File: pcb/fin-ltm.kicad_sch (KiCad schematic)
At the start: 68 parts, among them J1 Connector, USB-TYPE-C-16P, J2 Test Connector, J3 Display, Q1 MMBT3904, Q2 HL3415A, U1 ESP32-C3FH4, U2 RT9080, U3 SN74LV1T34DBV, X1 40MHz, 15pF

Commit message: pcb 2
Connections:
- net BRIGHTNESS_DOWN_BUTTON: now also R16.2, U1.15 (GPIO9); no longer R17.2, U1.16 (GPIO10)
- net BRIGHTNESS_UP_BUTTON: now also R17.2, U1.16 (GPIO10); no longer R16.2, U1.15 (GPIO9)
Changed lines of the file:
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@@
+	(wire
+		(pts
+			(xy 165.1 116.84) (xy 166.37 116.84)
+		)
+		(stroke
+			(width 0)
+			(type default)
+		)
+	)
+	(wire
+		(pts
+			(xy 236.22 34.29) (xy 236.22 35.56)
+		)
+		(stroke
+			(width 0)
+			(type default)
+		)
+	)
+	(wire
+		(pts
+			(xy 181.61 43.18) (xy 208.28 43.18)
+		)
+		(stroke
+			(width 0)
+			(type default)
+		)
+	)
 	(wire
 		(pts
 			(xy 165.1 50.8) (xy 208.28 50.8)
-		)
-		(stroke
-			(width 0)
-			(type default)
-		)
-	)
-	(wire
-		(pts
-			(xy 165.1 116.84) (xy 166.37 116.84)
-		)
-		(stroke
-			(width 0)
-			(type default)
-		)
-	)
-	(wire
-		(pts
-			(xy 236.22 34.29) (xy 236.22 35.56)
-		)
-		(stroke
-			(width 0)
-			(type default)
-		)
-	)
-	(wire
-		(pts
-			(xy 181.61 43.18) (xy 208.28 43.18)
 		)
 		(stroke
@@
 	)
 	(label "BRIGHTNESS_DOWN_BUTTON"
-		(at 181.61 50.8 0)
+		(at 181.61 48.26 0)
 		(effects
 			(font
@@
 	)
 	(label "BRIGHTNESS_UP_BUTTON"
-		(at 181.61 48.26 0)
-		(effects
-			(font
+		(at 181.61 50.8 0)
+		(effects
+			(font

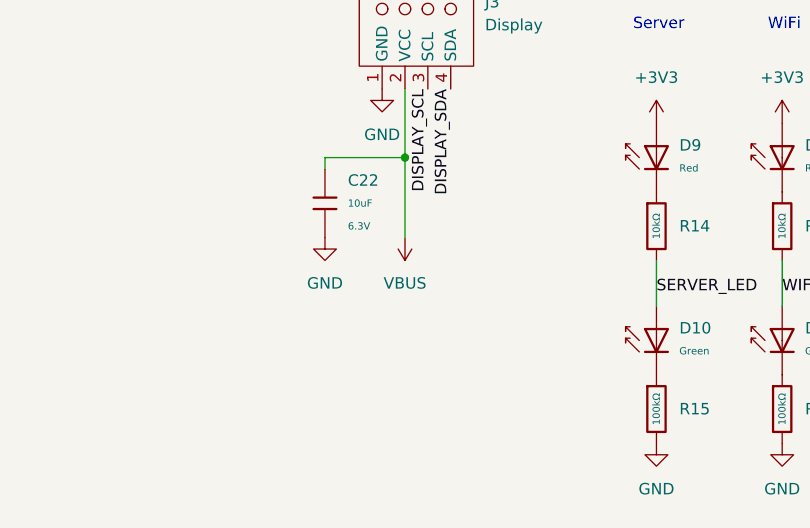
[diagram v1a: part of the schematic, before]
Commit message: add oled
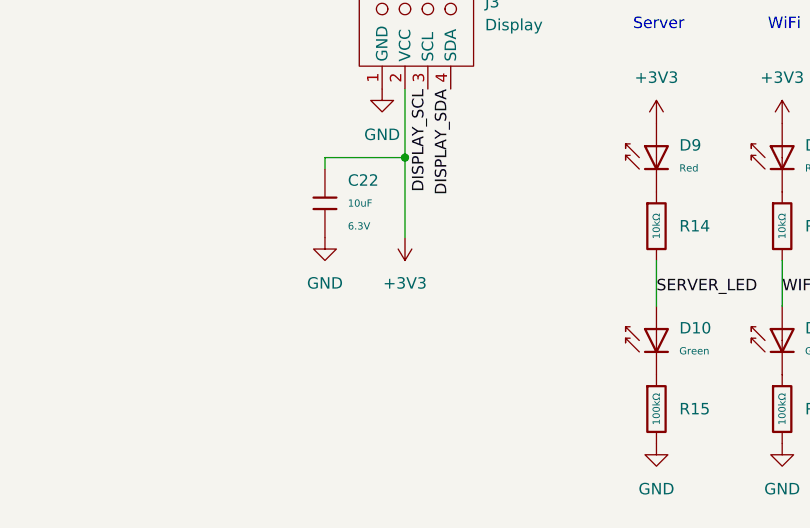
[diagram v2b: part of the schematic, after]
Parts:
- AE1: footprint Library:Inverted_F_Antenna_2.4Ghz_1.0mmPCB_TI_CC2430DB.pretty -> Custom:Inverted_F_Antenna_2.4Ghz_1.0mmPCB_TI_CC2430DB.pretty
- J2: footprint Library:Test_connector -> Custom:Test_connector
- J3: footprint (none) -> Custom:OLED_1306_THT_pinheader
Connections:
- net +3V3: now also C22.1, J3.2 (VCC)
- net VBUS: no longer C22.1, J3.2 (VCC)
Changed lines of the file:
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@@
 			)
 		)
-		(property "Footprint" "Library:Test_connector"
+		(property "Footprint" "Custom:Test_connector"
 			(at 269.24 106.68 0)
 			(hide yes)
@@
 	)
 	(symbol
+		(lib_id "power:+3V3")
+		(at 87.63 160.02 180)
+		(unit 1)
+		(body_style 1)
+		(exclude_from_sim no)
+		(in_bom yes)
+		(on_board yes)
+		(in_pos_files yes)
+		(dnp no)
+		(fields_autoplaced yes)
+		(property "Reference" "#PWR0302"
+			(at 87.63 156.21 0)
+			(hide yes)
+			(show_name no)
+			(do_not_autoplace no)
+			(effects
+				(font
+					(size 1.27 1.27)
+				)
+			)
+		)
+		(property "Value" "+3V3"
+			(at 87.63 165.1 0)
+			(show_name no)
+			(do_not_autoplace no)
+			(effects
+				(font
+					(size 1.27 1.27)
+				)
+			)
+		)
+		(property "Footprint" ""
+			(at 87.63 160.02 0)
+			(hide yes)
+			(show_name no)
+			(do_not_autoplace no)
+			(effects
+				(font
+					(size 1.27 1.27)
+				)
+			)
+		)
+		(property "Datasheet" ""
+			(at 87.63 160.02 0)
+			(hide yes)
+			(show_name no)
+			(do_not_autoplace no)
+			(effects
+				(font
+					(size 1.27 1.27)
+				)
+			)
+		)
+		(property "Description" "Power symbol creates a global label with name \"+3V3\""
+			(at 87.63 160.02 0)
+			(hide yes)
+			(show_name no)
+			(do_not_autoplace no)
+			(effects
+				(font
+					(size 1.27 1.27)
+				)
+			)
+		)
+		(pin "1"
+		)
+		(instances
+			(project "fin-ltm"
+				(path "/da13f94e-0fc0-403b-a3ae-59c6a026d422"
+					(reference "#PWR0302")
+					(unit 1)
+				)
+			)
+		)
+	)
+	(symbol
 		(lib_id "power:GND")
 		(at 165.1 124.46 0)
@@
 			)
 		)
-		(property "Footprint" "Library:Inverted_F_Antenna_2.4Ghz_1.0mmPCB_TI_CC2430DB.pretty"
+		(property "Footprint" "Custom:Inverted_F_Antenna_2.4Ghz_1.0mmPCB_TI_CC2430DB.pretty"
 			(at 194.31 109.22 0)
 			(hide yes)
@@
 			)
 		)
-		(property "Footprint" ""
+		(property "Footprint" "Custom:OLED_1306_THT_pinheader"
 			(at 88.9 140.97 0)
 			(hide yes)
@@
 					(unit 1)
 				)
-			)
-		)
-	)
-	(symbol
-		(lib_id "power:VBUS")
-		(at 87.63 160.02 180)
-		(unit 1)
-		(body_style 1)
-		(exclude_from_sim no)
-		(in_bom yes)
-		(on_board yes)
-		(in_pos_files yes)
-		(dnp no)
-		(fields_autoplaced yes)
-		(property "Reference" "#PWR075"
-			(at 87.63 156.21 0)
-			(hide yes)
-			(show_name no)
-			(do_not_autoplace no)
-			(effects
-				(font
-					(size 1.27 1.27)
-				)
-			)
-		)
-		(property "Value" "VBUS"
-			(at 87.63 165.1 0)
-			(show_name no)
-			(do_not_autoplace no)
-			(effects
-				(font
-					(size 1.27 1.27)
-				)
-			)
-		)
-		(property "Footprint" ""
-			(at 87.63 160.02 0)
-			(hide yes)
-			(show_name no)
-			(do_not_autoplace no)
-			(effects
-				(font
-					(size 1.27 1.27)
-				)
-			)
-		)
-		(property "Datasheet" ""
-			(at 87.63 160.02 0)
-			(hide yes)
-			(show_name no)
-			(do_not_autoplace no)
-			(effects
-				(font
-					(size 1.27 1.27)
-				)
-			)
-		)
-		(property "Description" "Power symbol creates a global label with name \"VBUS\""
-			(at 87.63 160.02 0)
-			(hide yes)
-			(show_name no)
-			(do_not_autoplace no)
-			(effects
-				(font
-					(size 1.27 1.27)
-				)
-			)
-		)
-		(pin "1"
-		)
-		(instances
-			(project "fin-ltm"
-				(path "/da13f94e-0fc0-403b-a3ae-59c6a026d422"
-					(reference "#PWR075")
-					(unit 1)
-				)

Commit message: led routing
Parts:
- removed C22: 10uF, PCM_JLCPCB:C_0402, symbol PCM_JLCPCB-Capacitors:0402,10uF
- removed J3: Display, Custom:OLED_1306_THT_pinheader, symbol New_Library:SSD1306_Conn
- removed R18, R19: 10kΩ, PCM_JLCPCB:R_0402, symbol PCM_JLCPCB-Resistors:0402,10kΩ
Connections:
- net DISPLAY_SCL: no longer names the net of U1.5 (GPIO1/XTAL_32K_N)
- net DISPLAY_SDA: no longer names the net of U1.4 (GPIO0/XTAL_32K_P)

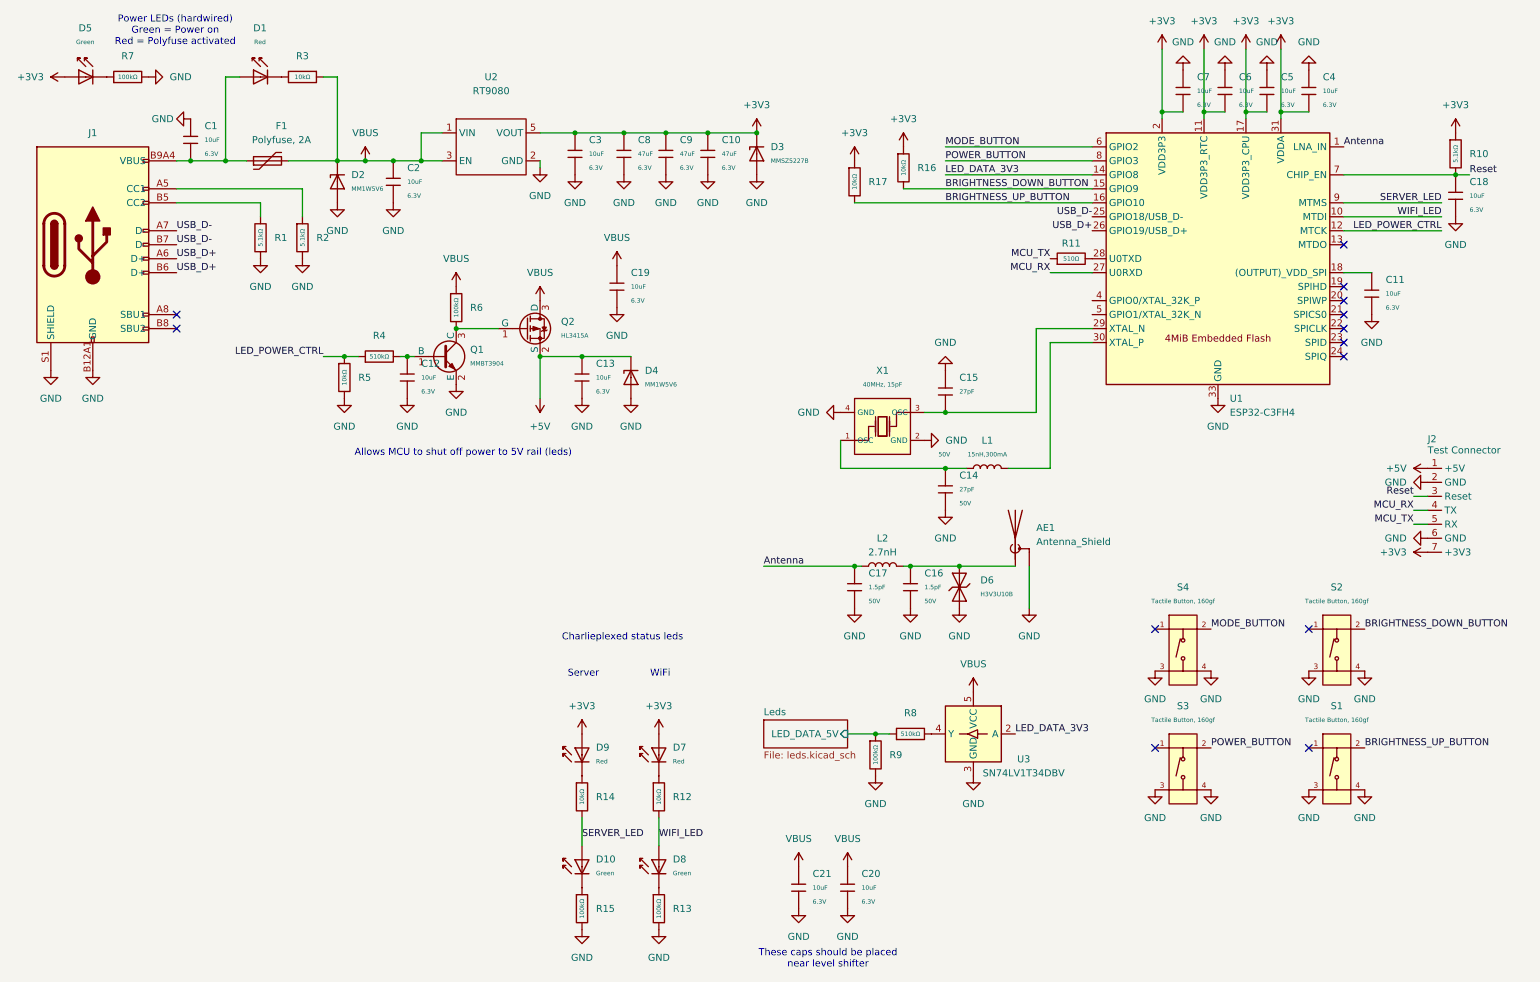
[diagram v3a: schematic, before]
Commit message: linking leds to stations
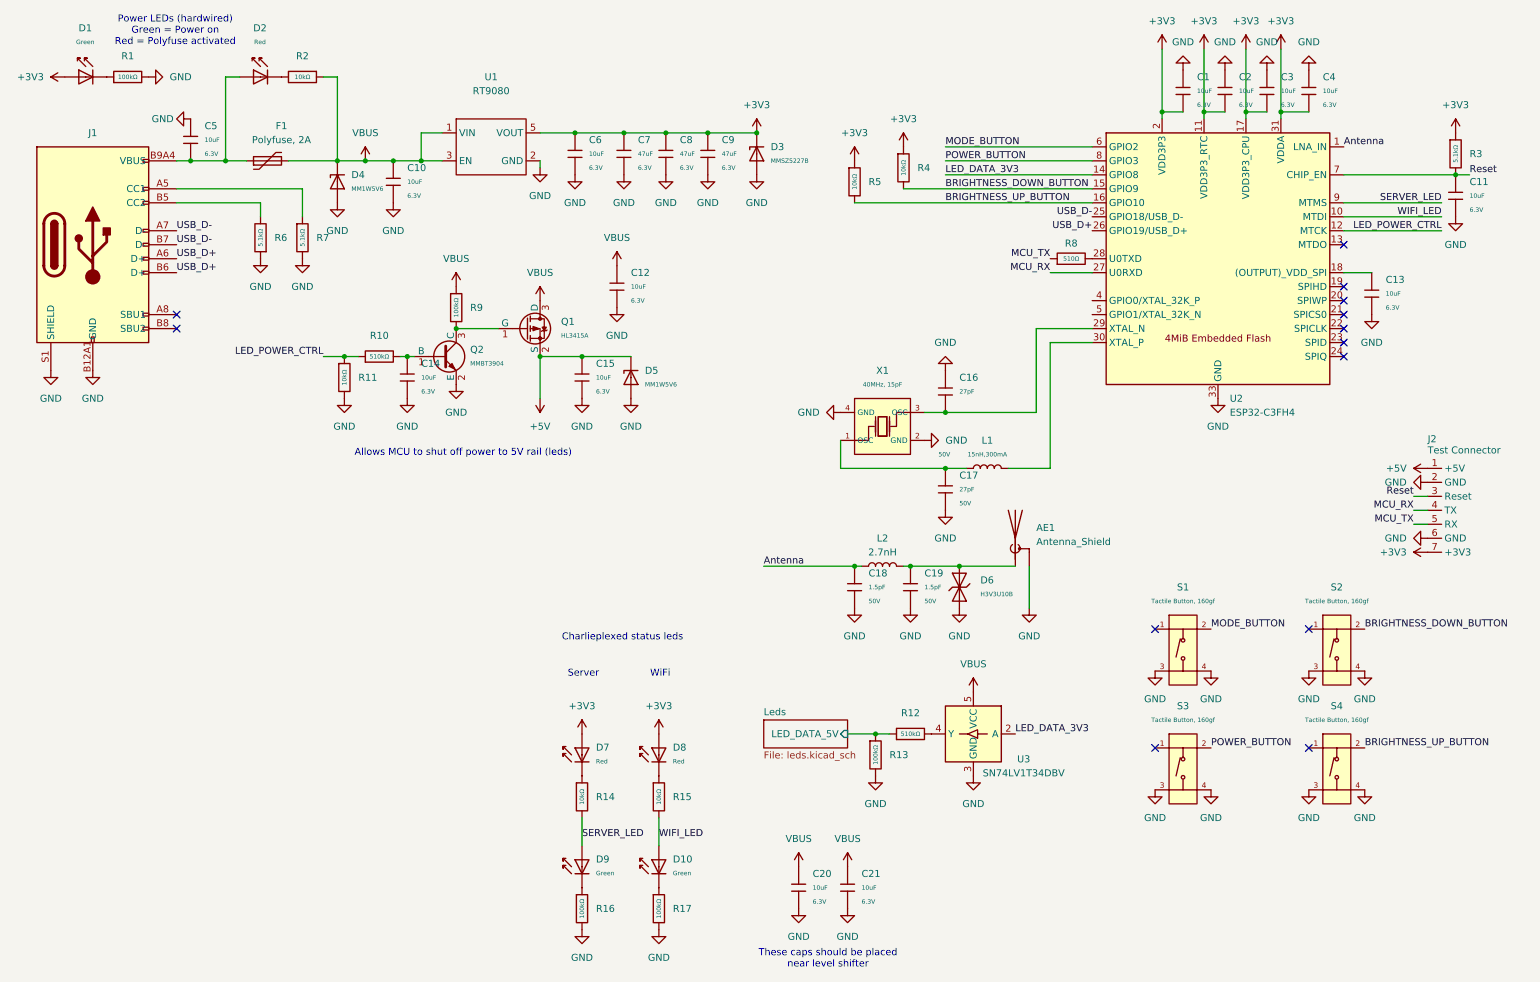
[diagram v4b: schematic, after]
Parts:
- renumbered C7 to C1, C2 to C10, C18 to C11, C19 to C12, C11 to C13, C12 to C14, C13 to C15, C15 to C16, C14 to C17, C17 to C18, C16 to C19, C6 to C2, C21 to C20, C20 to C21, C5 to C3, C1 to C5, C3 to C6, C8 to C7, C9 to C8, C10 to C9, D5 to D1, D8 to D10, D1 to D2, D2 to D4, D4 to D5, D9 to D7, D7 to D8, D10 to D9, Q2 to Q1, Q1 to Q2, R7 to R1, R4 to R10, R5 to R11, R8 to R12, R9 to R13, R12 to R15, R15 to R16, R13 to R17, R3 to R2, R10 to R3, R16 to R4, R17 to R5, R1 to R6, R2 to R7, R11 to R8, R6 to R9, S4 to S1, S1 to S4, U2 to U1, U1 to U2

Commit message: pcb finished
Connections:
- no-connect marks 13 -> 15
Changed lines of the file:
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@@
+	)
+	(no_connect
+		(at 208.28 68.58)
 	)
 	(no_connect
@@
 	)
 	(no_connect
+		(at 208.28 71.12)
+	)
+	(no_connect

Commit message: finished pcb
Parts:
- C10, C12, C20, C21, C5: footprint PCM_JLCPCB:C_0402 -> PCM_JLCPCB:C_0603; symbol PCM_JLCPCB-Capacitors:0402,10uF -> PCM_JLCPCB-Capacitors:0603,10uF; LCSC C15525 -> C19702; Part CL05A106MQ5NUNC -> CL10A106KP8NNNC; Stock 3940889 -> 9881407; Tolerance ±20% -> ±10%; Voltage Rated 6.3V -> 10V
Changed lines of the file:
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@@
 	)
 	(symbol
-		(lib_id "PCM_JLCPCB-Capacitors:0402,10uF")
+		(lib_id "PCM_JLCPCB-Capacitors:0603,10uF")
 		(at 154.94 175.26 0)
 		(unit 1)
@@
 			)
 		)
-		(property "Footprint" "PCM_JLCPCB:C_0402"
+		(property "Footprint" "PCM_JLCPCB:C_0603"
 			(at 153.162 175.26 90)
 			(hide yes)
@@
 			)
 		)
-		(property "Datasheet" "https://www.lcsc.com/datasheet/lcsc_datasheet_2208231630_Samsung-Electro-Mechanics-CL05A106MQ5NUNC_C15525.pdf"
+		(property "Datasheet" "https://www.lcsc.com/datasheet/lcsc_datasheet_2304140030_Samsung-Electro-Mechanics-CL10A106KP8NNNC_C19702.pdf"
 			(at 154.94 175.26 0)
 			(hide yes)
@@
 			)
 		)
-		(property "Description" "6.3V 10uF X5R ±20% 0402 Multilayer Ceramic Capacitors MLCC - SMD/SMT ROHS"
+		(property "Description" "10V 10uF X5R ±10% 0603 Multilayer Ceramic Capacitors MLCC - SMD/SMT ROHS"
 			(at 154.94 175.26 0)
 			(hide yes)
@@
 			)
 		)
-		(property "LCSC" "C15525"
+		(property "LCSC" "C19702"
 			(at 154.94 175.26 0)
 			(hide yes)
@@
 			)
 		)
-		(property "Stock" "3940889"
+		(property "Stock" "9881407"
 			(at 154.94 175.26 0)
 			(hide yes)
@@
 			)
 		)
-		(property "Part" "CL05A106MQ5NUNC"
+		(property "Part" "CL10A106KP8NNNC"
 			(at 154.94 175.26 0)
 			(hide yes)
@@
 			)
 		)
-		(property "Voltage Rated" "6.3V"
+		(property "Voltage Rated" "10V"
 			(at 157.48 177.8 0)
 			(show_name no)
@@
 			)
 		)
-		(property "Tolerance" "±20%"
+		(property "Tolerance" "±10%"
 			(at 154.94 175.26 0)
 			(hide yes)
@@
 	)
 	(symbol
-		(lib_id "PCM_JLCPCB-Capacitors:0402,10uF")
+		(lib_id "PCM_JLCPCB-Capacitors:0603,10uF")
 		(at 163.83 175.26 0)
 		(unit 1)
@@
 			)
 		)
-		(property "Footprint" "PCM_JLCPCB:C_0402"
+		(property "Footprint" "PCM_JLCPCB:C_0603"
 			(at 162.052 175.26 90)
 			(hide yes)
@@
 			)
 		)
-		(property "Datasheet" "https://www.lcsc.com/datasheet/lcsc_datasheet_2208231630_Samsung-Electro-Mechanics-CL05A106MQ5NUNC_C15525.pdf"
+		(property "Datasheet" "https://www.lcsc.com/datasheet/lcsc_datasheet_2304140030_Samsung-Electro-Mechanics-CL10A106KP8NNNC_C19702.pdf"
 			(at 163.83 175.26 0)
 			(hide yes)
@@
 			)
 		)
-		(property "Description" "6.3V 10uF X5R ±20% 0402 Multilayer Ceramic Capacitors MLCC - SMD/SMT ROHS"
+		(property "Description" "10V 10uF X5R ±10% 0603 Multilayer Ceramic Capacitors MLCC - SMD/SMT ROHS"
 			(at 163.83 175.26 0)
 			(hide yes)
@@
 			)
 		)
-		(property "LCSC" "C15525"
+		(property "LCSC" "C19702"
 			(at 163.83 175.26 0)
 			(hide yes)
@@
 			)
 		)
-		(property "Stock" "3940889"
+		(property "Stock" "9881407"
 			(at 163.83 175.26 0)
 			(hide yes)
@@
 			)
 		)
-		(property "Part" "CL05A106MQ5NUNC"
+		(property "Part" "CL10A106KP8NNNC"
 			(at 163.83 175.26 0)
 			(hide yes)
@@
 			)
 		)
-		(property "Voltage Rated" "6.3V"
+		(property "Voltage Rated" "10V"
 			(at 166.37 177.8 0)
 			(show_name no)
@@
 			)
 		)
-		(property "Tolerance" "±20%"
+		(property "Tolerance" "±10%"
 			(at 163.83 175.26 0)
 			(hide yes)
@@
 	)
 	(symbol
-		(lib_id "PCM_JLCPCB-Capacitors:0402,10uF")
+		(lib_id "PCM_JLCPCB-Capacitors:0603,10uF")
 		(at 81.28 46.99 0)
 		(unit 1)
@@
 		)
 		(property "Value" "10uF"
-			(at 83.82 46.99 0)
+			(at 83.312 47.3682 0)
 			(show_name no)
 			(do_not_autoplace no)
@@
 			)
 		)
-		(property "Footprint" "PCM_JLCPCB:C_0402"
+		(property "Footprint" "PCM_JLCPCB:C_0603"
 			(at 79.502 46.99 90)
 			(hide yes)
@@
 			)
 		)
-		(property "Datasheet" "https://www.lcsc.com/datasheet/lcsc_datasheet_2208231630_Samsung-Electro-Mechanics-CL05A106MQ5NUNC_C15525.pdf"
+		(property "Datasheet" "https://www.lcsc.com/datasheet/lcsc_datasheet_2304140030_Samsung-Electro-Mechanics-CL10A106KP8NNNC_C19702.pdf"
 			(at 81.28 46.99 0)
 			(hide yes)
@@
 			)
 		)
-		(property "Description" "6.3V 10uF X5R ±20% 0402 Multilayer Ceramic Capacitors MLCC - SMD/SMT ROHS"
+		(property "Description" "10V 10uF X5R ±10% 0603 Multilayer Ceramic Capacitors MLCC - SMD/SMT ROHS"
 			(at 81.28 46.99 0)
 			(hide yes)
@@
 			)
 		)
-		(property "LCSC" "C15525"
+		(property "LCSC" "C19702"
 			(at 81.28 46.99 0)
 			(hide yes)
@@
 			)
 		)
-		(property "Stock" "3940889"
+		(property "Stock" "9881407"
 			(at 81.28 46.99 0)
 			(hide yes)
@@
 			)
 		)
-		(property "Part" "CL05A106MQ5NUNC"
+		(property "Part" "CL10A106KP8NNNC"
 			(at 81.28 46.99 0)
 			(hide yes)
@@
 			)
 		)
-		(property "Voltage Rated" "6.3V"
-			(at 83.82 49.53 0)
+		(property "Voltage Rated" "10V"
+			(at 83.312 49.0362 0)
 			(show_name no)
 			(do_not_autoplace no)
@@
 			)
 		)
-		(property "Tolerance" "±20%"
+		(property "Tolerance" "±10%"
 			(at 81.28 46.99 0)
 			(hide yes)
@@
 	)
 	(symbol
-		(lib_id "PCM_JLCPCB-Capacitors:0402,10uF")
+		(lib_id "PCM_JLCPCB-Capacitors:0603,10uF")
 		(at 44.45 39.37 0)
 		(unit 1)
@@
 		)
 		(property "Value" "10uF"
-			(at 46.99 39.37 0)
+			(at 46.482 39.7482 0)
 			(show_name no)
 			(do_not_autoplace no)
@@
 			)
 		)
-		(property "Footprint" "PCM_JLCPCB:C_0402"
+		(property "Footprint" "PCM_JLCPCB:C_0603"
 			(at 42.672 39.37 90)
 			(hide yes)
@@
 			)
 		)
-		(property "Datasheet" "https://www.lcsc.com/datasheet/lcsc_datasheet_2208231630_Samsung-Electro-Mechanics-CL05A106MQ5NUNC_C15525.pdf"
+		(property "Datasheet" "https://www.lcsc.com/datasheet/lcsc_datasheet_2304140030_Samsung-Electro-Mechanics-CL10A106KP8NNNC_C19702.pdf"
 			(at 44.45 39.37 0)
 			(hide yes)
@@
 			)
 		)
-		(property "Description" "6.3V 10uF X5R ±20% 0402 Multilayer Ceramic Capacitors MLCC - SMD/SMT ROHS"
+		(property "Description" "10V 10uF X5R ±10% 0603 Multilayer Ceramic Capacitors MLCC - SMD/SMT ROHS"
 			(at 44.45 39.37 0)
 			(hide yes)
@@
 			)
 		)
-		(property "LCSC" "C15525"
+		(property "LCSC" "C19702"
 			(at 44.45 39.37 0)
 			(hide yes)
@@
 			)
 		)
-		(property "Stock" "3940889"
+		(property "Stock" "9881407"
 			(at 44.45 39.37 0)
 			(hide yes)
@@
 			)
 		)
-		(property "Part" "CL05A106MQ5NUNC"
+		(property "Part" "CL10A106KP8NNNC"
 			(at 44.45 39.37 0)
 			(hide yes)
@@
 			)
 		)
-		(property "Voltage Rated" "6.3V"
-			(at 46.99 41.91 0)
+		(property "Voltage Rated" "10V"
+			(at 46.482 41.4162 0)
 			(show_name no)
 			(do_not_autoplace no)
@@
 			)
 		)
-		(property "Tolerance" "±20%"
+		(property "Tolerance" "±10%"
 			(at 44.45 39.37 0)
 			(hide yes)
@@
 	)
 	(symbol
-		(lib_id "PCM_JLCPCB-Capacitors:0402,10uF")
+		(lib_id "PCM_JLCPCB-Capacitors:0603,10uF")
 		(at 121.92 66.04 0)
 		(unit 1)
@@
 			)
 		)
-		(property "Footprint" "PCM_JLCPCB:C_0402"
+		(property "Footprint" "PCM_JLCPCB:C_0603"
 			(at 120.142 66.04 90)
 			(hide yes)
@@
 			)
 		)
-		(property "Datasheet" "https://www.lcsc.com/datasheet/lcsc_datasheet_2208231630_Samsung-Electro-Mechanics-CL05A106MQ5NUNC_C15525.pdf"
+		(property "Datasheet" "https://www.lcsc.com/datasheet/lcsc_datasheet_2304140030_Samsung-Electro-Mechanics-CL10A106KP8NNNC_C19702.pdf"
 			(at 121.92 66.04 0)
 			(hide yes)
@@
 			)
 		)
-		(property "Description" "6.3V 10uF X5R ±20% 0402 Multilayer Ceramic Capacitors MLCC - SMD/SMT ROHS"
+		(property "Description" "10V 10uF X5R ±10% 0603 Multilayer Ceramic Capacitors MLCC - SMD/SMT ROHS"
 			(at 121.92 66.04 0)
 			(hide yes)
@@
 			)
 		)
-		(property "LCSC" "C15525"
+		(property "LCSC" "C19702"
 			(at 121.92 66.04 0)
 			(hide yes)
@@
 			)
 		)
-		(property "Stock" "3940889"
+		(property "Stock" "9881407"
 			(at 121.92 66.04 0)
 			(hide yes)
@@
 			)
 		)
-		(property "Part" "CL05A106MQ5NUNC"
+		(property "Part" "CL10A106KP8NNNC"
 			(at 121.92 66.04 0)
 			(hide yes)
@@
 			)
 		)
-		(property "Voltage Rated" "6.3V"
+		(property "Voltage Rated" "10V"
 			(at 124.46 68.58 0)
 			(show_name no)
@@
 			)
 		)
-		(property "Tolerance" "±20%"
+		(property "Tolerance" "±10%"
 			(at 121.92 66.04 0)
 			(hide yes)
